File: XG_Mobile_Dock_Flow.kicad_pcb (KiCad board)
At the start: 4 copper layers, 220 x 65 mm, 57 parts, among them J1 5-1775443-8, J10 SWD, J11 UART, J12 I2C1, J13 39300240, J14 469911008, J17 8730, J2 20455-040E-76, J3 20455-040E-76, J4 3-2362375-4, J5 USB_C_Receptacle, Q16 AO3401A, Q17 2N7002W, SW1 SW_Push, U12 STM32F030C8Tx

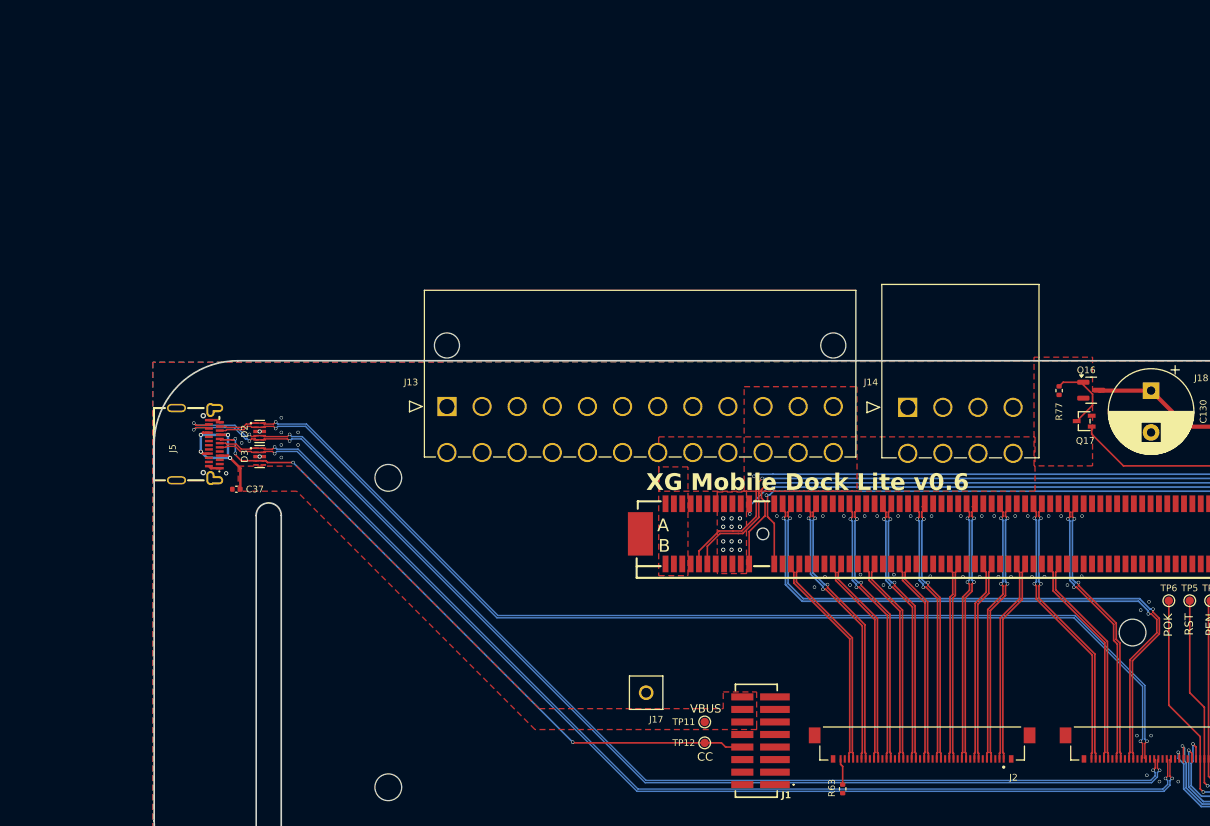
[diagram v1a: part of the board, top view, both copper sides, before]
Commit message: more changes in pcb, initial layout of the pci connections for redriver
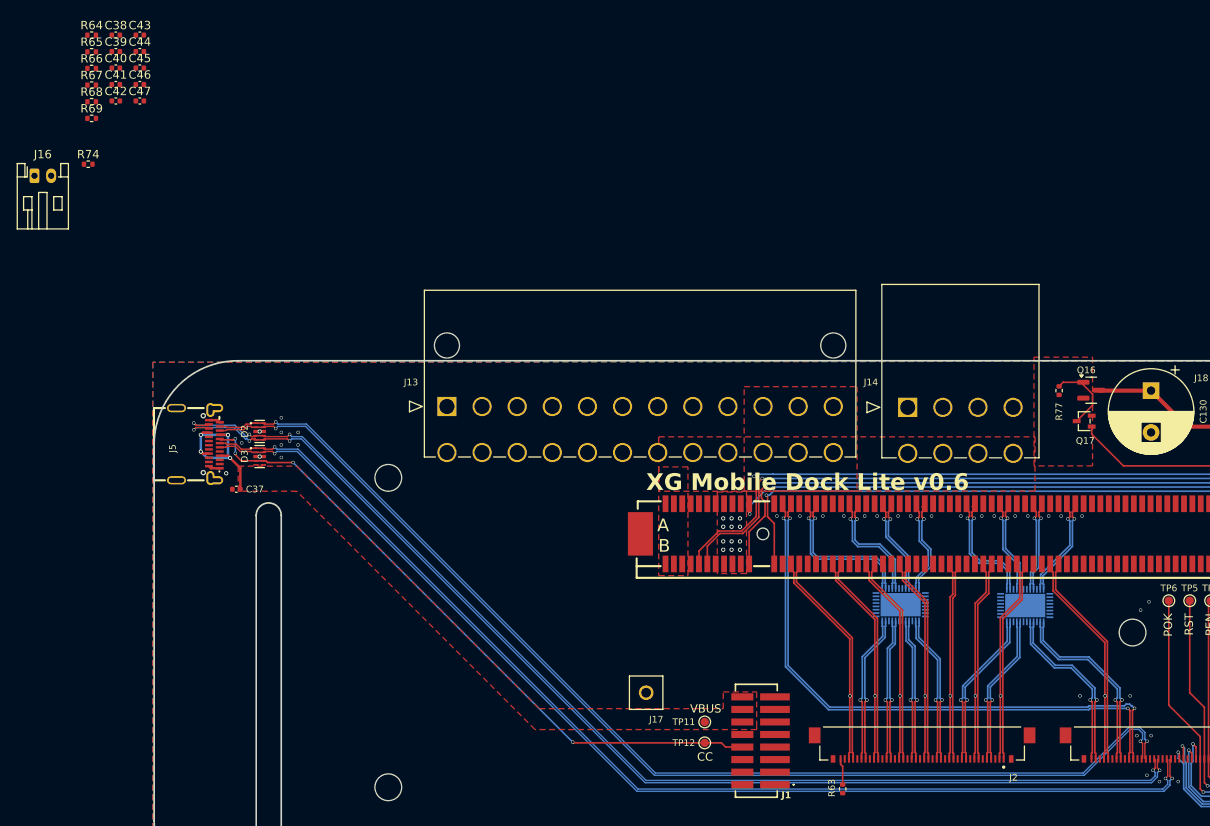
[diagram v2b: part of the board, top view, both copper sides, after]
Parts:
- added C38: 0.1μF, Capacitor_SMD:C_0402_1005Metric, F.Cu at (12.2, 0.48)
- added C39: 0.1μF, Capacitor_SMD:C_0402_1005Metric, F.Cu at (12.2, 2.46)
- added C40: 0.1μF, Capacitor_SMD:C_0402_1005Metric, F.Cu at (12.2, 4.42)
- added C41: 0.1μF, Capacitor_SMD:C_0402_1005Metric, F.Cu at (12.2, 6.39)
- added C42: 1μF, Capacitor_SMD:C_0402_1005Metric, F.Cu at (12.2, 8.37)
- added C43: 0.1μF, Capacitor_SMD:C_0402_1005Metric, F.Cu at (15.1, 0.48)
- added C44: 0.1μF, Capacitor_SMD:C_0402_1005Metric, F.Cu at (15.1, 2.46)
- added C45: 0.1μF, Capacitor_SMD:C_0402_1005Metric, F.Cu at (15.1, 4.42)
- added C46: 0.1μF, Capacitor_SMD:C_0402_1005Metric, F.Cu at (15.1, 6.39)
- added C47: 1μF, Capacitor_SMD:C_0402_1005Metric, F.Cu at (15.1, 8.37)
- added J16: ~, Connector_JST:JST_PH_S2B-PH-K_1x02_P2.00mm_Horizontal, F.Cu at (2.48, 17.3)
- added R64: 59k, Resistor_SMD:R_0402_1005Metric, F.Cu at (9.31, 0.49)
- added R65: 59k, Resistor_SMD:R_0402_1005Metric, F.Cu at (9.31, 2.48)
- added R66: 59k, Resistor_SMD:R_0402_1005Metric, F.Cu at (9.31, 4.47)
- added R67: 59k, Resistor_SMD:R_0402_1005Metric, F.Cu at (9.31, 6.46)
- added R68: 1k, Resistor_SMD:R_0402_1005Metric, F.Cu at (9.31, 8.46)
- added R69: 1k, Resistor_SMD:R_0402_1005Metric, F.Cu at (9.31, 10.4)
- added R74: 47k, Resistor_SMD:R_0402_1005Metric, F.Cu at (8.90, 15.9)
- added U1: DS160PR410RNQR, DS160PR410RNQR:WQFN_RNQ40_TEX, B.Cu at (120.9, 68.7)
- added U2: DS160PR410RNQR, DS160PR410RNQR:WQFN_RNQ40_TEX, B.Cu at (106.1, 68.6)
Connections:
- J2 pad 10: /HSI4N -> /HSIL4N
- J2 pad 11: /HSI4P -> /HSIL4P
- J2 pad 16: /HSI3N -> /HSIL3N
- J2 pad 17: /HSI3P -> /HSIL3P
- J2 pad 22: /HSI2N -> /HSIL2N
- J2 pad 23: /HSI2P -> /HSIL2P
- J2 pad 28: /HSI1N -> /HSIL1N
- J2 pad 29: /HSI1P -> /HSIL1P
- J2 pad 34: /HSI0N -> /HSIL0N
- J2 pad 35: /HSI0P -> /HSIL0P
- J2 pad 4: /HSI5N -> /HSIL5N
- J2 pad 5: /HSI5P -> /HSIL5P
- J3 pad 33: /HSI7N -> /HSIL7N
- J3 pad 34: /HSI7P -> /HSIL7P
- J3 pad 39: /HSI6N -> /HSIL6N
- J3 pad 40: /HSI6P -> /HSIL6P
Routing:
- net /HSI6P: track 33.9 -> 10.9 mm, vias 2 -> 1
- net /HSI6N: track 34.0 -> 11.0 mm, vias 2 -> 1
- net /HSIL7N: track 0.00 -> 22.5 mm, vias 0 -> 1
- net /HSIL7P: track 0.00 -> 22.5 mm, vias 0 -> 1
- net /HSI7N: track 33.6 -> 12.2 mm, vias 2 -> 1
- net /HSI7P: track 33.5 -> 12.0 mm, vias 2 -> 1
- net /HSI2N: track 32.6 -> 11.6 mm, vias 2 -> 1
- net /HSI2P: track 32.4 -> 11.5 mm, vias 2 -> 1
- net /HSIL6N: track 0.00 -> 20.9 mm, vias 0 -> 1
- net /HSIL6P: track 0.00 -> 20.9 mm, vias 0 -> 1
- net /HSI5P: track 31.9 -> 11.3 mm, vias 2 -> 1
- net /HSI5N: track 31.9 -> 11.3 mm, vias 2 -> 1
- net /HSI3P: track 32.0 -> 11.5 mm, vias 2 -> 1
- net /HSI3N: track 32.3 -> 11.8 mm, vias 2 -> 1
- net /HSI1N: track 32.8 -> 14.0 mm, vias 2 -> 1
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
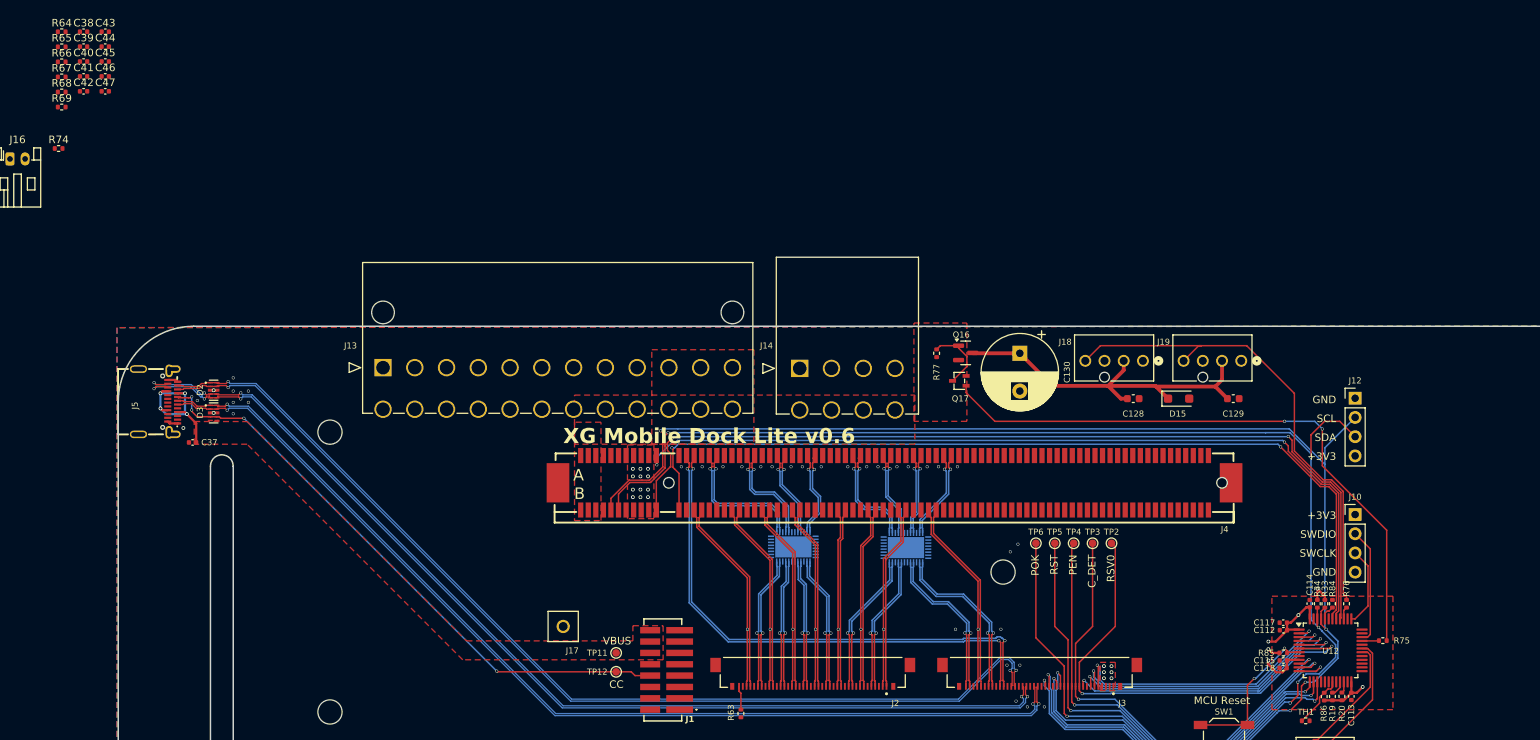
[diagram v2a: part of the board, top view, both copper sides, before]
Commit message: almost finished adding power inputs to redrivers
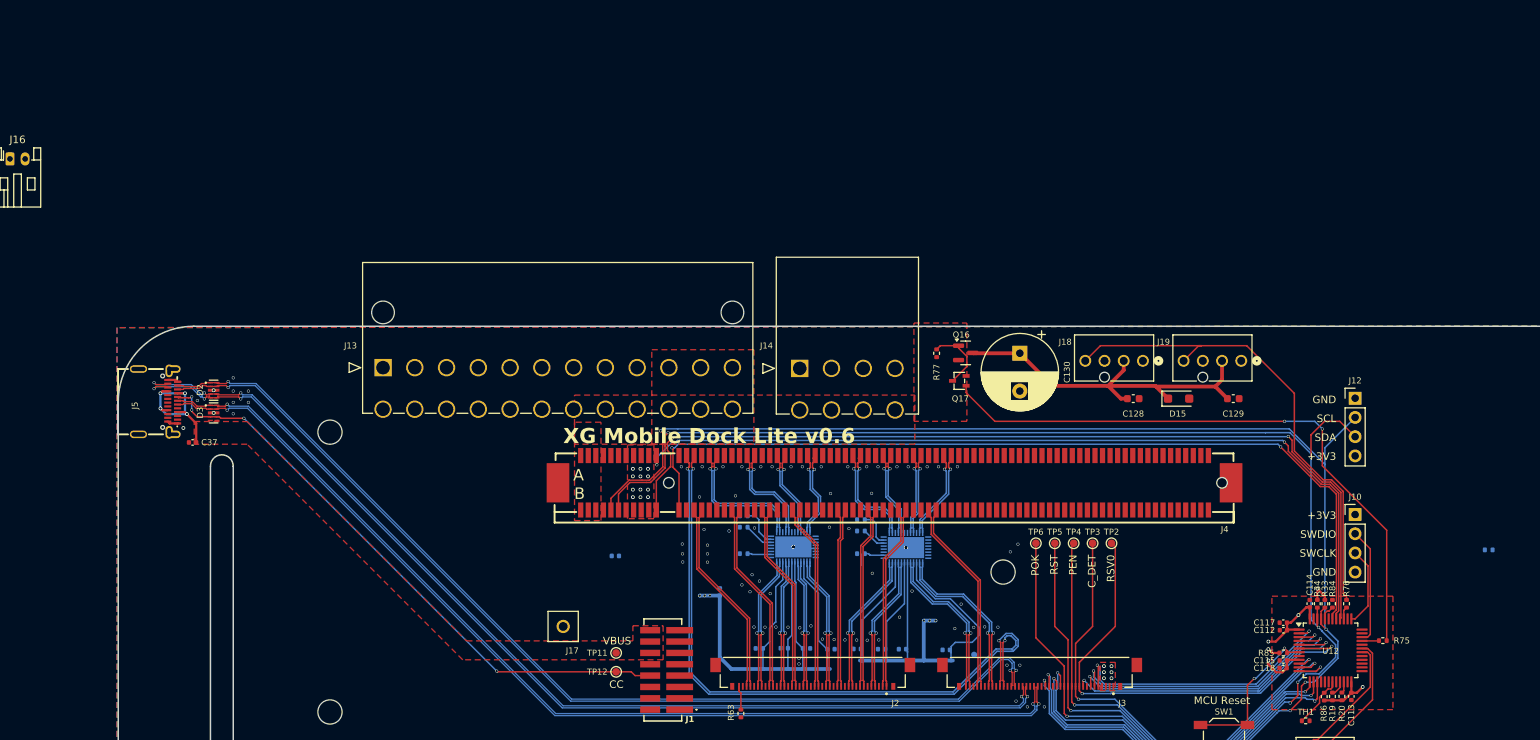
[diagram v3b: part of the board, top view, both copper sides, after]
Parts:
- C38, C39, C40, C41, C42, C43, C44, C45, C46, C47, R64, R65, R66, R67, R68, R69, R74: moved to B.Cu
- moved R74 196.4 mm to (198.0, 69.0), turned to 180 degrees
- moved C43 138.0 mm to (126.3, 82.2), turned to 180 degrees
- moved C38 133.4 mm to (117.7, 82.1), turned to 180 degrees
- moved C40 133.3 mm to (120.5, 82.1), turned to 180 degrees
- moved C39 129.6 mm to (114.5, 82.1), turned to 180 degrees
- moved C41 124.5 mm to (111.0, 82.1)
- moved R66 122.5 mm to (115.0, 66.5), turned to 180 degrees
- moved R69 121.1 mm to (115.0, 69.5), turned to 180 degrees
- moved C45 120.9 mm to (107.8, 82.0)
- moved R67 120.8 mm to (115.0, 65.0), turned to 180 degrees
- moved C44 117.5 mm to (101.6, 82.0), turned to 180 degrees
- moved C46 117.4 mm to (104.9, 82.0), turned to 180 degrees
- moved R64 111.5 mm to (99.5, 66.0), turned to 180 degrees
- moved R65 109.4 mm to (99.5, 64.5), turned to 180 degrees
- moved R68 108.9 mm to (99.5, 69.5), turned to 180 degrees
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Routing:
- net +3V3: track 143.4 -> 337.2 mm, vias 24 -> 30
- net /CLKP: track 69.3 -> 87.0 mm
- net /CLKN: track 69.9 -> 84.8 mm
- net /U2_EQ_ADDR2: track 0.00 -> 5.33 mm
- net /U1_EQ_ADDR2: track 0.00 -> 4.68 mm
- net GND: track 6.51 -> 11.0 mm, vias 44 -> 84
- net /U2_EQ_ADDR1: track 0.00 -> 3.94 mm
- net /U2_EN_SMB: track 0.00 -> 3.29 mm
- net /U1_EQ_ADDR1: track 0.00 -> 3.16 mm
- net /U1_EN_SMB: track 0.00 -> 2.58 mm

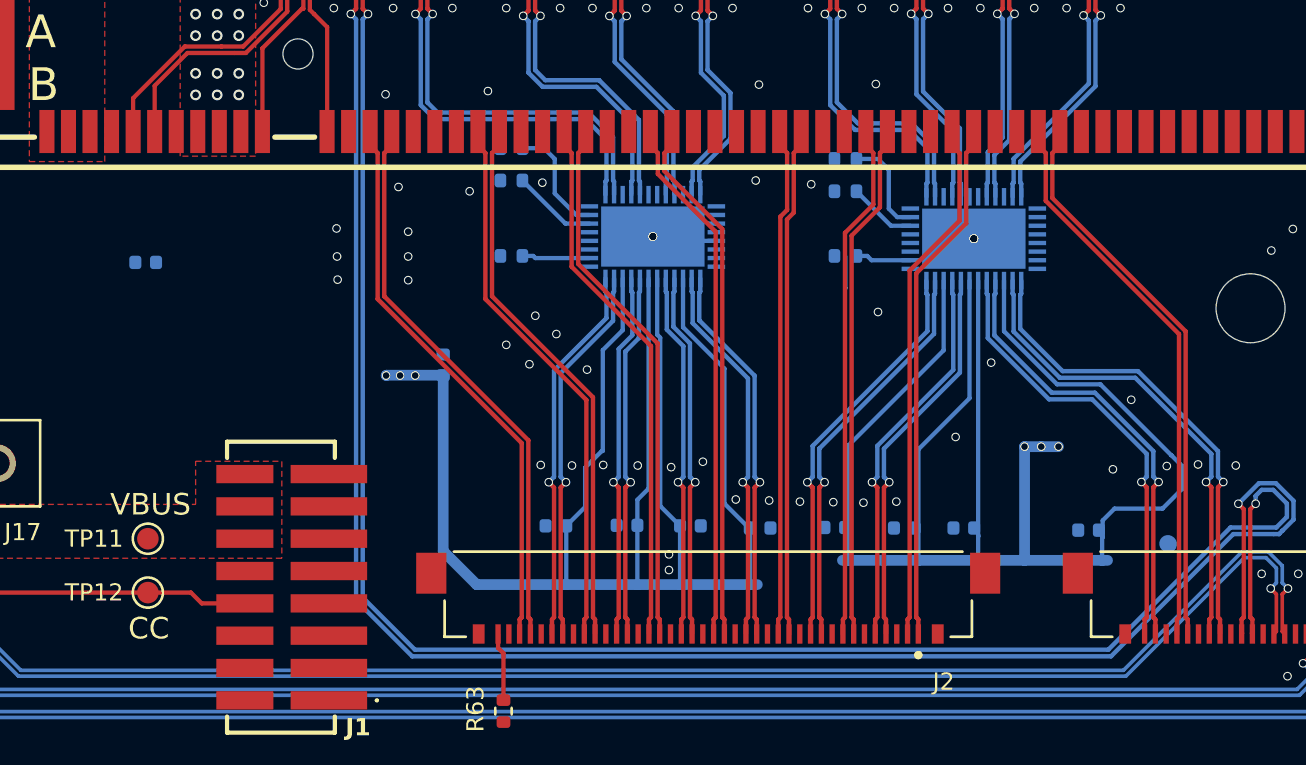
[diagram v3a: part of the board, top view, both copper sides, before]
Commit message: added proper pads for redrivers for ground
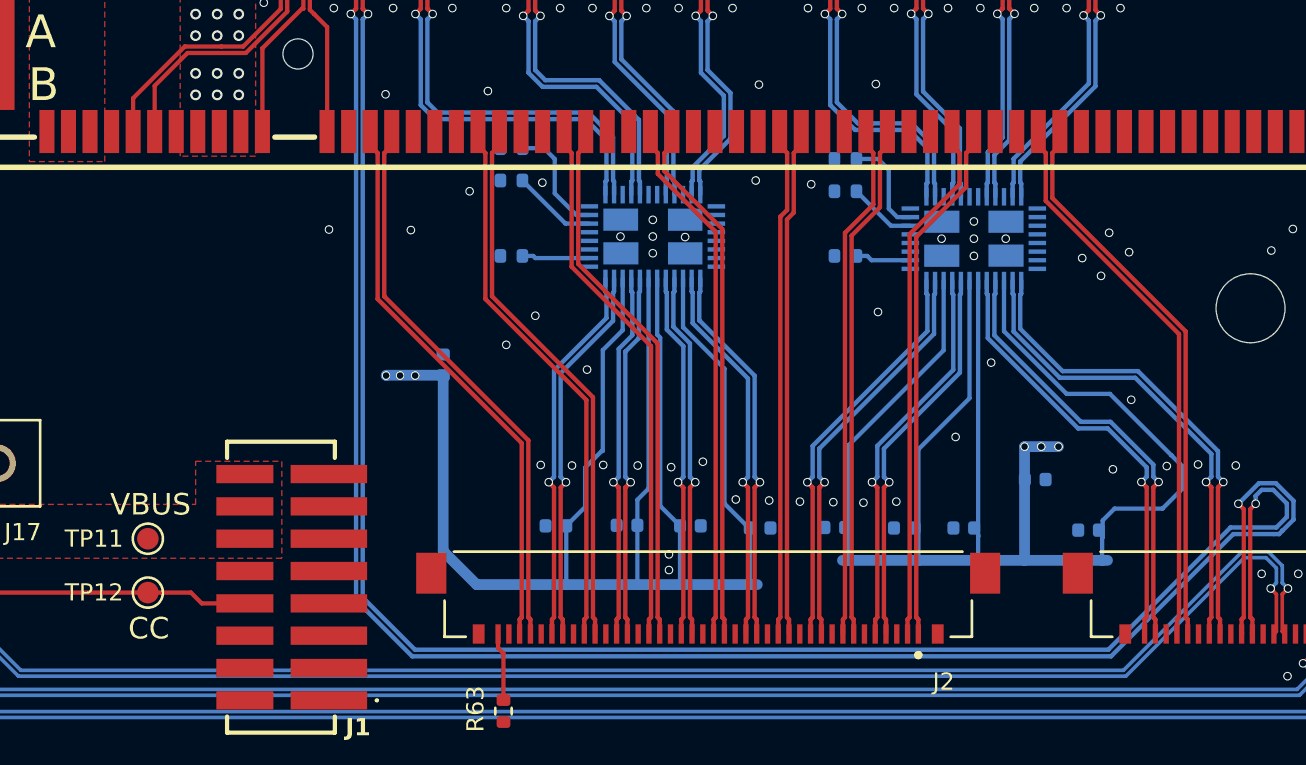
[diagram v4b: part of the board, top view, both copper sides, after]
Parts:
- moved C47 42.5 mm to (123.8, 79.9), turned to 0 degrees
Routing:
- net GND: track 11.0 -> 6.51 mm, vias 84 -> 83

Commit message: fixed issues and almost final implementation
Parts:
- added C48: 0.1μF, Capacitor_SMD:C_0402_1005Metric, F.Cu at (109.0, 66.6)
- added C49: 0.1μF, Capacitor_SMD:C_0402_1005Metric, F.Cu at (105.1, 66.6)
- added C50: 0.1μF, Capacitor_SMD:C_0402_1005Metric, F.Cu at (123.1, 66.9)
- added C51: 0.1μF, Capacitor_SMD:C_0402_1005Metric, F.Cu at (118.4, 66.2)
- C38, C39, C40, C41, C43, C44, C45, C46: moved to F.Cu
- moved C44 11.7 mm to (104.1, 70.6), turned to 90 degrees
- moved C40 11.4 mm to (121.6, 70.8), turned to 0 degrees
- moved C45 11.2 mm to (106.7, 70.8)
- moved C39 10.4 mm to (119.6, 73.0), turned to -90 degrees
- moved C43 9.95 mm to (122.3, 73.1), turned to -90 degrees
- moved C41 9.80 mm to (107.5, 73.0), turned to -90 degrees
- moved C38 9.03 mm to (120.8, 73.6), turned to -90 degrees
- moved C46 9.02 mm to (105.4, 73.0)
- moved C47 0.20 mm to (123.8, 80.1)
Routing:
- net +3V3: track 337.2 -> 346.6 mm, vias 30 -> 38
- net /U2_VREG0: track 0.00 -> 2.97 mm, vias 0 -> 1
- net /U1_VREG0: track 0.00 -> 1.82 mm, vias 0 -> 1
- net /U1_VREG1: track 0.00 -> 1.71 mm, vias 0 -> 1
- net /U2_VREG1: track 0.00 -> 1.41 mm, vias 0 -> 1
- net GND: vias 83 -> 98
